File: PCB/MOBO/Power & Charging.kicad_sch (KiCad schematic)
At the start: 45 parts, among them J201 USB_C_Receptacle_PowerOnly_6P, Q1 Si4435DDY, Q2 IRLML6344, Q3 NMOS, Q4 NMOS, SW1 SW_DPST_x2, U1 BQ297xy, U202 MCP73871-1AA, U205 TPS61230DRC

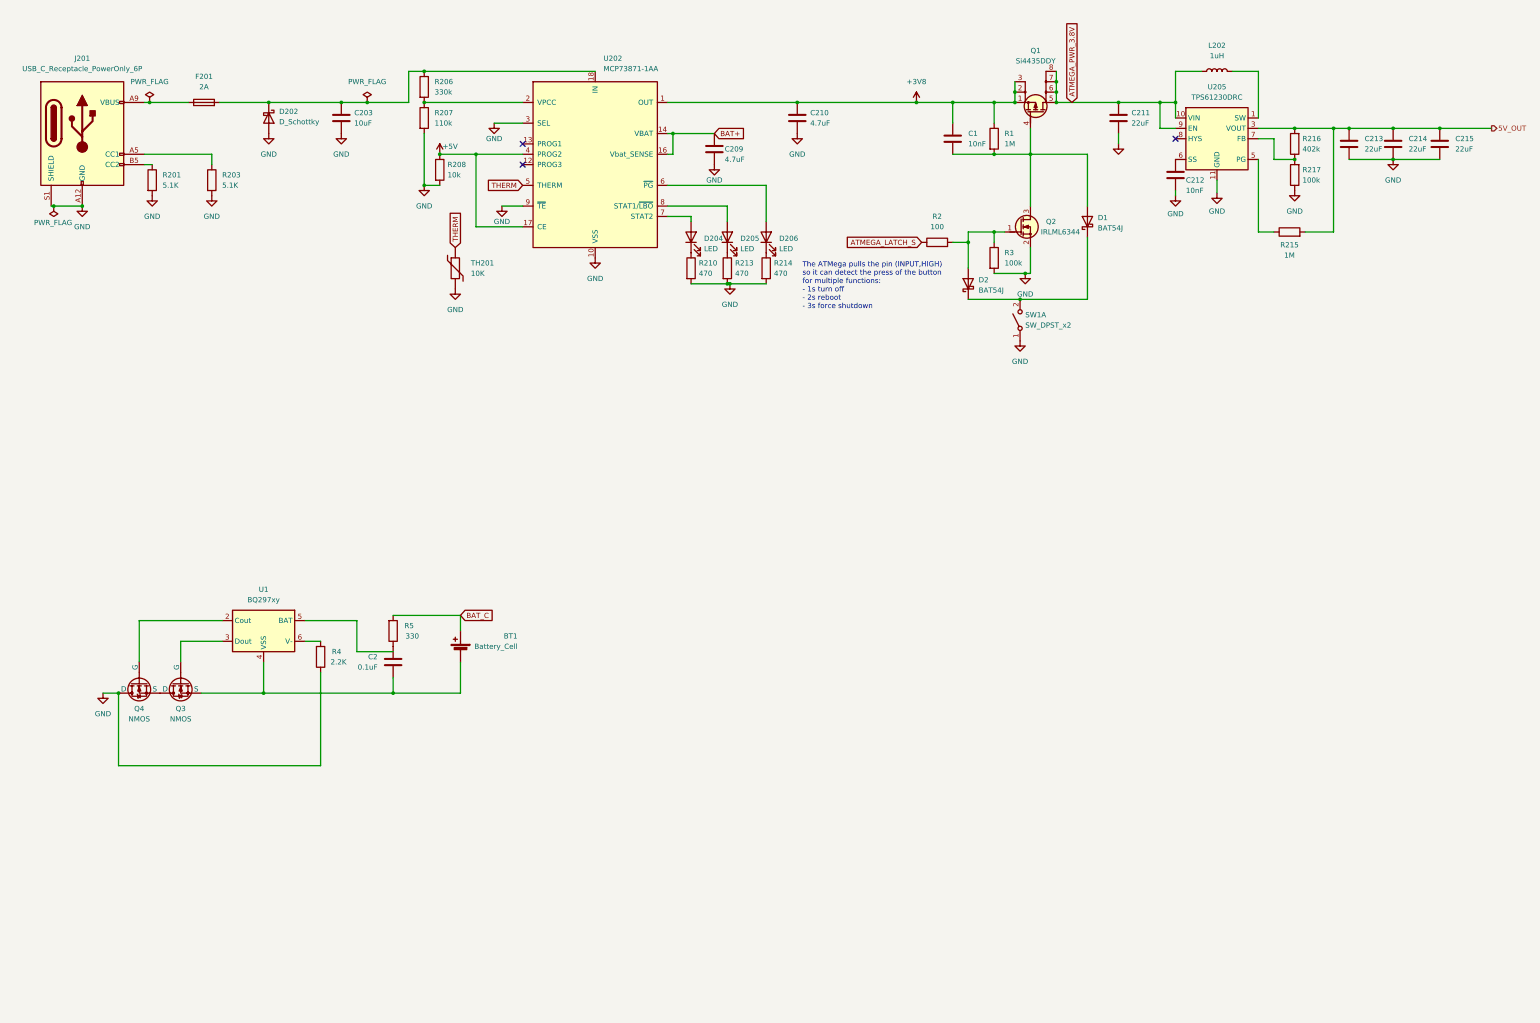
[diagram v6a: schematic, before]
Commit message: Completed protection circuit Added:  - LC709203F i2c battery fuel gauge  - Fixed MCP73871 charging current  - Added reverse protection mosfet on main usb power rail  - Added thermistor to MCP73871
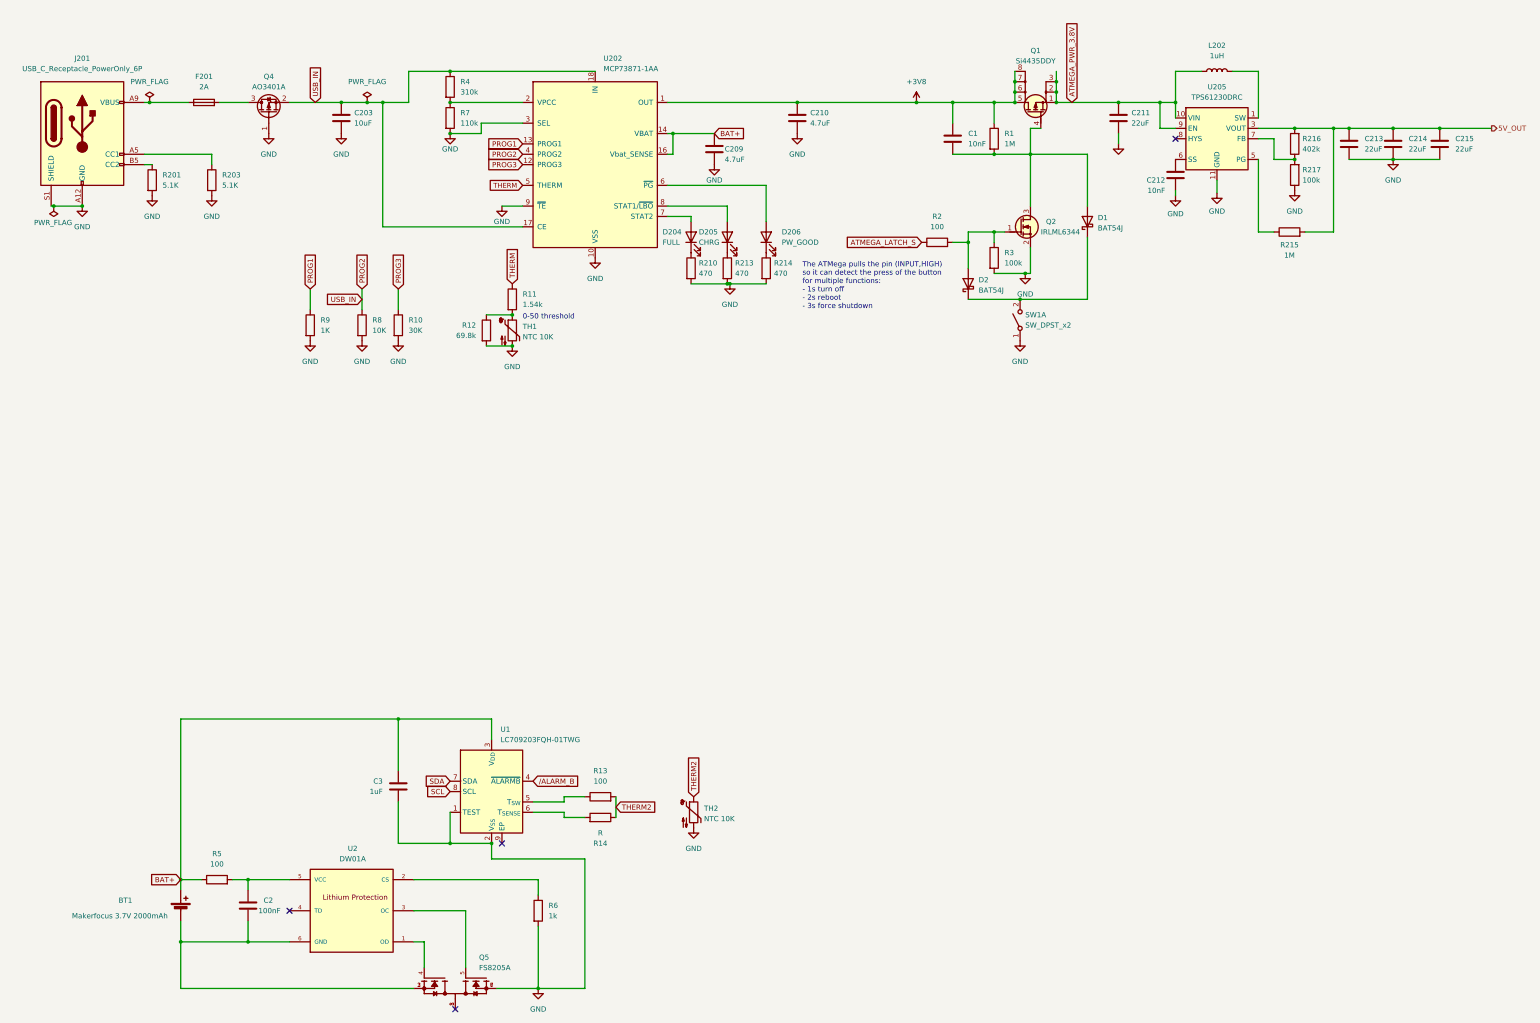
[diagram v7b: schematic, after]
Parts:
- removed D202: D_Schottky, symbol Device:D_Schottky
- removed Q3, Q4: NMOS, symbol Simulation_SPICE:NMOS
- removed R206: 330k, symbol Device:R
- removed R207: 110k, symbol Device:R
- removed R208: 10k, symbol Device:R
- removed TH201: 10K, symbol Device:Thermistor
- removed U1: BQ297xy, Package_SON:WSON-6_1.5x1.5mm_P0.5mm, symbol Battery_Management:BQ297xy
- added C3: 1uF, symbol Device:C
- added Q4: AO3401A, Package_TO_SOT_SMD:SOT-23, symbol Transistor_FET:AO3401A
- added Q5: FS8205A, FS8205A:SOP65P640X120-8N, symbol FS8205A:FS8205A
- added R10: 30K, symbol Device:R
- added R11: 1.54k, symbol Device:R
- added R12: 69.8k, symbol Device:R
- added R13: 100, symbol Device:R
- added R14: R, symbol Device:R
- added R6: 1k, symbol Device:R
- added R7: 110k, symbol Device:R
- added R8: 10K, symbol Device:R
- added R9: 1K, symbol Device:R
- added TH1, TH2: NTC 10K, symbol Device:Thermistor_NTC
- added U1: LC709203FQH-01TWG, Package_DFN_QFN:WDFN-8-1EP_4x3mm_P0.65mm_EP2.4x1.8mm, symbol Battery_Management:LC709203FQH-01TWG
- added U2: DW01A, DW01A:SOT23-6, symbol DW01A:DW01A
- BT1: value Battery_Cell -> Makerfocus 3.7V 2000mAh
- C2: value 0.1uF -> 100nF
- D204: value LED -> FULL
- D205: value LED -> CHRG
- D206: value LED -> PW_GOOD
- R4: value 2.2K -> 310k
- R5: value 330 -> 100
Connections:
- net +5V is gone; now on net PROG2: U202.17 (CE), U202.4 (PROG2)
- net +3V8: now also Q1.5 (D), Q1.6 (D), Q1.7 (D), Q1.8 (D); no longer Q1.1 (S), Q1.2 (S), Q1.3 (S)
- net ATMEGA_PWR_3.8V: now also Q1.1 (S), Q1.2 (S), Q1.3 (S); no longer Q1.5 (D), Q1.6 (D), Q1.7 (D), Q1.8 (D)
- net BAT+: now also BT1.1 (+), R5.1, C3.1, U1.3 (V_{DD})
- net GND: now also C3.2, Q4.1 (G), Q5.6, Q5.7, R10.2, R12.2, R6.2, R7.2, R8.2, R9.2, TH1.2, TH2.2, U1.1 (TEST), U1.2 (V_{SS}); no longer R4.1
- net THERM: now also R11.1
- net PROG3: now reaches U202.12 (PROG3)
- net PROG3: now also R10.1
- net PROG1: now reaches U202.13 (PROG1)
- net PROG1: now also R9.1
- net PROG2: now reaches C203.1, U202.18 (IN), U202.19 (IN)
- net PROG2: now also R4.1, Q4.2 (S), R8.1; no longer F201.2
- net at U202.2 (VPCC): now also R4.2, R7.1
- net at C2.1: now also R5.2, U2.5 (VCC); no longer R5.1
- net at BT1.2 (-), C2.2: now also Q5.2, Q5.3, U2.6 (GND)
- removed net BAT_C: BT1.1 (+), R5.2
- new net: F201.2, Q4.3 (D)
- new net: R13.1, U1.5 (T_{SW})
- new net: R11.2, R12.1, TH1.1
- new net: R6.1, U2.2 (CS)
- new net: R14.2, U1.6 (T_{SENSE})
- new net: Q5.1, Q5.8
- new net: Q5.4, U2.1 (OD)
- new net: Q5.5, U2.3 (OC)
- new net SCL: U1.8 (SCL)
- new net SDA: U1.7 (SDA)
- new net THERM2: R13.2, R14.1, TH2.1
- new net /ALARM_B: U1.4 (~{ALARMB})
- no-connect marks 3 -> 4
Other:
- note added: "0-50 threshold"
- moved on the sheet: BT1, Q1

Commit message: added full atmega circuit and programming interface
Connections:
- net ATMEGA_PWR_3.8V renamed 3.8V_OUT
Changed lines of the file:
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@@
-    )
-  )
-  (global_label "ATMEGA_PWR_3.8V" (shape input) (at 271.78 36.83 90) (fields_autoplaced)
-    (effects (font (size 1.27 1.27)) (justify left))
-    (property "Intersheetrefs" "${INTERSHEET_REFS}" (at 271.78 16.7906 90)
-      (effects (font (size 1.27 1.27)) (justify left) hide)
     )
   )
@@
     )
   )
+  (hierarchical_label "3.8V_OUT" (shape input) (at 278.13 36.83 90) (fields_autoplaced)
+    (effects (font (size 1.27 1.27)) (justify left))
+  )
   (hierarchical_label "5V_OUT" (shape output) (at 374.65 43.18 0) (fields_autoplaced)
